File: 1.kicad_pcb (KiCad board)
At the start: 2 copper layers, 85.1 x 45.7 mm, 52 parts, among them J1 USB_B_Micro, J10 SPI2, J11 Micro_SD_Card, J12 Conn_01x04, J2 Power, J3 SWD, J4 Conn_01x02, J5 ADC, J6 SPI1, J7 UART1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

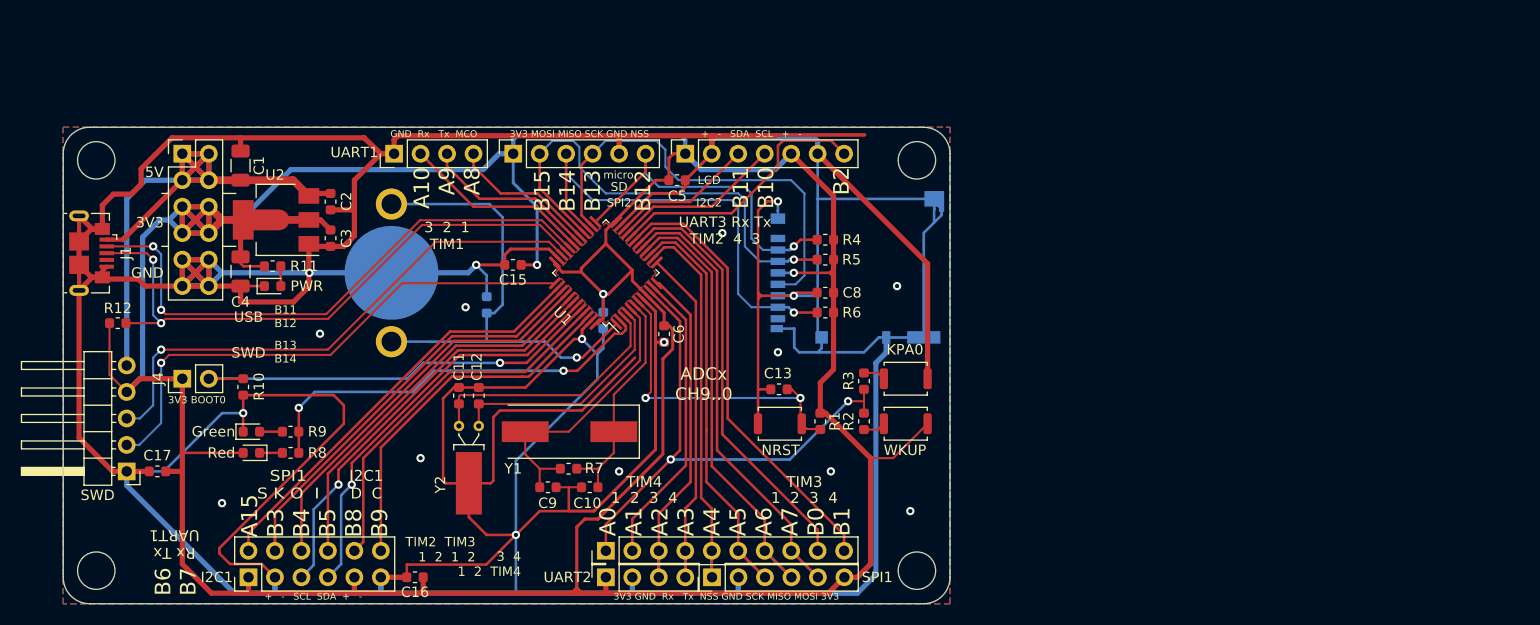
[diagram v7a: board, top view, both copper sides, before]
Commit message: line wider to 0.5mm, move micro sd lines
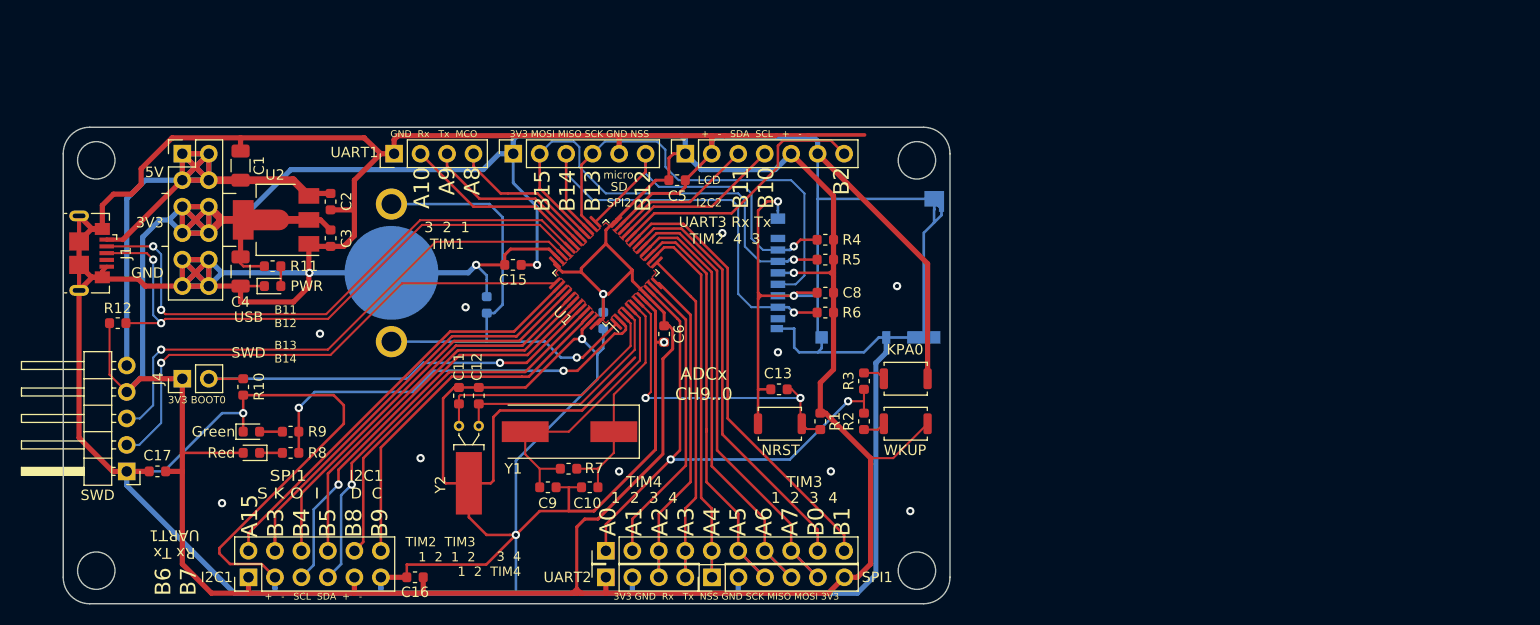
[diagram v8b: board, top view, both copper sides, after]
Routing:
- net /PB15: track 45.8 -> 45.0 mm
- removed copper zone on B.Cu, net GND
- removed copper zone on F.Cu, net GND
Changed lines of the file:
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@@
     (thickness 1.6)
     (drawings 82)
-    (tracks 779)
+    (tracks 777)
     (zones 0)
     (modules 52)
@@
   )
   (setup
-    (last_trace_width 0.75)
+    (last_trace_width 0.2)
     (user_trace_width 0.2)
     (user_trace_width 0.29)
@@
   (segment (start 62.992 105.664) (end 63.246 105.41) (width 0.5) (layer F.Cu) (net 3))
   (segment (start 62.992 108.96) (end 62.992 105.664) (width 0.5) (layer F.Cu) (net 3))
-  (segment (start 89.154 97.71) (end 89.154 99.06) (width 0.4) (layer B.Cu) (net 3))
-  (segment (start 89.529011 97.334989) (end 89.154 97.71) (width 0.4) (layer B.Cu) (net 3))
-  (segment (start 105.288989 97.334989) (end 89.529011 97.334989) (width 0.4) (layer B.Cu) (net 3))
-  (segment (start 105.664 97.71) (end 105.288989 97.334989) (width 0.4) (layer B.Cu) (net 3))
-  (segment (start 105.664 99.06) (end 105.664 97.71) (width 0.4) (layer B.Cu) (net 3))
+  (segment (start 89.154 97.71) (end 89.154 99.06) (width 0.5) (layer B.Cu) (net 3))
+  (segment (start 89.529011 97.334989) (end 89.154 97.71) (width 0.5) (layer B.Cu) (net 3))
+  (segment (start 105.288989 97.334989) (end 89.529011 97.334989) (width 0.5) (layer B.Cu) (net 3))
+  (segment (start 105.664 97.71) (end 105.288989 97.334989) (width 0.5) (layer B.Cu) (net 3))
+  (segment (start 105.664 99.06) (end 105.664 97.71) (width 0.5) (layer B.Cu) (net 3))
   (segment (start 94.742 141.224) (end 95.25 141.224) (width 0.5) (layer F.Cu) (net 3))
   (segment (start 95.25 141.224) (end 95.758 141.224) (width 0.5) (layer F.Cu) (net 3))
@@
   (segment (start 103.759 100.33) (end 105.029 101.6) (width 0.2) (layer B.Cu) (net 45))
   (segment (start 103.759 98.679) (end 103.759 100.33) (width 0.2) (layer B.Cu) (net 45))
-  (segment (start 97.999001 97.834999) (end 102.914999 97.834999) (width 0.2) (layer B.Cu) (net 45))
-  (segment (start 102.914999 97.834999) (end 103.759 98.679) (width 0.2) (layer B.Cu) (net 45))
-  (segment (start 96.774 99.06) (end 97.999001 97.834999) (width 0.2) (layer B.Cu) (net 45))
   (segment (start 95.708731 104.972751) (end 96.691658 105.955678) (width 0.25) (layer F.Cu) (net 45))
   (segment (start 95.708731 100.125269) (end 95.708731 104.972751) (width 0.25) (layer F.Cu) (net 45))
   (segment (start 96.774 99.06) (end 95.708731 100.125269) (width 0.25) (layer F.Cu) (net 45))
+  (segment (start 96.774 99.06) (end 97.949001 97.884999) (width 0.2) (layer B.Cu) (net 45))
+  (segment (start 102.964999 97.884999) (end 103.759 98.679) (width 0.2) (layer B.Cu) (net 45))
+  (segment (start 97.949001 97.884999) (end 102.964999 97.884999) (width 0.2) (layer B.Cu) (net 45))
   (segment (start 91.694 102.372234) (end 91.694 99.06) (width 0.25) (layer F.Cu) (net 46))
   (segment (start 95.984551 106.662785) (end 91.694 102.372234) (width 0.25) (layer F.Cu) (net 46))
@@
   (via (at 116.078 109.22) (size 0.8) (drill 0.4) (layers F.Cu B.Cu) (net 46))
   (segment (start 116.078 109.22) (end 118.313 109.22) (width 0.25) (layer F.Cu) (net 46))
+  (segment (start 111.379 103.505) (end 111.379 107.95) (width 0.2) (layer B.Cu) (net 46))
+  (segment (start 110.744 102.87) (end 111.379 103.505) (width 0.2) (layer B.Cu) (net 46))
   (segment (start 111.379 107.95) (end 112.819 109.39) (width 0.2) (layer B.Cu) (net 46))
-  (segment (start 95.504 98.425) (end 95.504 100.33) (width 0.2) (layer B.Cu) (net 46))
-  (segment (start 95.504 100.33) (end 98.044 102.87) (width 0.2) (layer B.Cu) (net 46))
   (segment (start 98.044 102.87) (end 110.744 102.87) (width 0.2) (layer B.Cu) (net 46))
+  (segment (start 95.504 100.33) (end 98.044 102.87) (width 0.2) (layer B.Cu) (net 46))
+  (segment (start 95.504 98.425) (end 95.504 100.33) (width 0.2) (layer B.Cu) (net 46))
+  (segment (start 94.963999 97.884999) (end 95.504 98.425) (width 0.2) (layer B.Cu) (net 46))
+  (segment (start 92.869001 97.884999) (end 94.963999 97.884999) (width 0.2) (layer B.Cu) (net 46))
   (segment (start 112.819 109.39) (end 114.549 109.39) (width 0.2) (layer B.Cu) (net 46))
-  (segment (start 110.744 102.87) (end 111.379 103.505) (width 0.2) (layer B.Cu) (net 46))
-  (segment (start 111.379 103.505) (end 111.379 107.95) (width 0.2) (layer B.Cu) (net 46))
-  (segment (start 91.694 99.06) (end 91.694 98.552) (width 0.2) (layer B.Cu) (net 46))
-  (segment (start 91.927992 98.407788) (end 92.140124 98.407788) (width 0.25) (layer F.Cu) (net 46))
-  (segment (start 94.913999 97.834999) (end 95.504 98.425) (width 0.2) (layer B.Cu) (net 46))
-  (segment (start 91.694 99.06) (end 92.919001 97.834999) (width 0.2) (layer B.Cu) (net 46))
-  (segment (start 92.919001 97.834999) (end 94.913999 97.834999) (width 0.2) (layer B.Cu) (net 46))
+  (segment (start 91.694 99.06) (end 92.869001 97.884999) (width 0.2) (layer B.Cu) (net 46))
   (segment (start 101.854 99.627081) (end 101.854 98.425) (width 0.25) (layer F.Cu) (net 47))
   (segment (start 114.635 108.204) (end 114.549 108.29) (width 0.25) (layer B.Cu) (net 47))
@@
       )
     )
-  )
-  (zone (net 2) (net_name GND) (layer B.Cu) (hatch edge 0.508)
-    (connect_pads (clearance 0.508))
-    (min_thickness 0.254)
-    (fill yes (arc_segments 32) (thermal_gap 0.508) (thermal_bridge_width 0.508))
-    (polygon
-      (pts
-        (xy 131.064 142.24) (xy 45.974 142.24) (xy 45.974 96.52) (xy 131.064 96.52)
-      )
-    )
-  )
-  (zone (net 2) (net_name GND) (layer F.Cu) (hatch edge 0.508)
-    (connect_pads (clearance 0.508))
-    (min_thickness 0.254)
-    (fill yes (arc_segments 32) (thermal_gap 0.508) (thermal_bridge_width 0.508))
-    (polygon
-      (pts
-        (xy 131.064 142.24) (xy 45.974 142.24) (xy 45.974 96.52) (xy 131.064 96.52)
-      )
-    )
